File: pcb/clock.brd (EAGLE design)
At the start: 76.2 x 25.4 mm, 20 parts, among them IC1 74AHCT125, U1 ESP-01, U2 LD1117V33

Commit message: Added DTR to RST pin
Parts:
- added C5: 0.1uF, rcl:C025-025X050
- added R7: 10K, rcl:0207/10
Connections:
- removed net N$2: R2.1, U1.B2, U1.C2
- new net N$4: R2.1, U1.B2
- new net RESET: C5.1, R7.1, U1.C2
- net DTR: now also C5.2
- net VCC: now also R7.2
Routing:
- net DTR: track 0.00 -> 34.4 mm
- net RESET: track 0.00 -> 18.5 mm
- net N$4: track 0.00 -> 13.8 mm
- net N$2: track 13.8 -> 0.00 mm
- net VCC: track 57.1 -> 60.3 mm
- net GPIO0: track 32.8 -> 31.8 mm
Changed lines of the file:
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@@
 <setting verticaltext="up"/>
 </settings>
-<grid distance="0.05" unitdist="inch" unit="inch" style="lines" multiple="1" display="yes" altdistance="0.025" altunitdist="inch" altunit="inch"/>
+<grid distance="0.05" unitdist="inch" unit="inch" style="lines" multiple="1" display="yes" altdistance="0.005" altunitdist="inch" altunit="inch"/>
 <layers>
 <layer number="1" name="Top" color="4" fill="1" visible="yes" active="yes"/>
@@
 <element name="H1" library="holes" package="2,8-PAD" value="MOUNT-PAD-ROUND2.8" x="62.865" y="20.32"/>
 <element name="H2" library="holes" package="2,8-PAD-SQUARE" value="MOUNT-PAD-SQUARE2.8" x="71.12" y="20.32"/>
-<element name="D1" library="diode" package="DO41-7.6" value="1N5817-B" x="20.32" y="9.525" rot="R180"/>
+<element name="D1" library="diode" package="DO41-7.6" value="1N5817-B" x="20.32" y="9.525" smashed="yes" rot="R180"/>
+<element name="R7" library="rcl" package="0207/10" value="10K" x="40.64" y="8.89" smashed="yes">
+<attribute name="VALUE" x="38.3794" y="8.255" size="1.27" layer="27" ratio="10"/>
+</element>
+<element name="C5" library="rcl" package="C025-025X050" value="0.1uF" x="33.02" y="8.89" smashed="yes" rot="R270"/>
 </elements>
 <signals>
@@
 <wire x1="51.435" y1="5.715" x2="52.07" y2="5.08" width="0.4064" layer="1"/>
 <wire x1="45.72" y1="2.54" x2="45.72" y2="5.715" width="0.4064" layer="1"/>
+<contactref element="R7" pad="2"/>
+<wire x1="45.72" y1="8.89" x2="45.72" y2="5.715" width="0.4064" layer="1"/>
 </signal>
 <signal name="+5V">
@@
 <signal name="DTR">
 <contactref element="JP1" pad="6"/>
+<contactref element="C5" pad="2"/>
+<wire x1="2.54" y1="5.08" x2="2.54" y2="3.81" width="0.4064" layer="16"/>
+<wire x1="2.54" y1="3.81" x2="3.81" y2="2.54" width="0.4064" layer="16"/>
+<wire x1="3.81" y1="2.54" x2="17.78" y2="2.54" width="0.4064" layer="16"/>
+<wire x1="17.78" y1="2.54" x2="19.05" y2="3.81" width="0.4064" layer="16"/>
+<wire x1="19.05" y1="3.81" x2="29.21" y2="3.81" width="0.4064" layer="16"/>
+<wire x1="29.21" y1="3.81" x2="33.02" y2="7.62" width="0.4064" layer="16"/>
 </signal>
 <signal name="RXD_3V3">
@@
 <wire x1="24.13" y1="22.86" x2="26.67" y2="20.32" width="0.4064" layer="16"/>
 </signal>
-<signal name="N$2">
-<contactref element="U1" pad="B2"/>
-<contactref element="R2" pad="1"/>
-<contactref element="U1" pad="C2"/>
-<wire x1="22.86" y1="2.54" x2="25.4" y2="2.54" width="0.4064" layer="1"/>
-<wire x1="25.4" y1="2.54" x2="26.67" y2="3.81" width="0.4064" layer="1"/>
-<wire x1="26.67" y1="3.81" x2="34.29" y2="3.81" width="0.4064" layer="1"/>
-<wire x1="34.29" y1="3.81" x2="35.56" y2="2.54" width="0.4064" layer="1"/>
-</signal>
 <signal name="N$3">
 <contactref element="R4" pad="1"/>
@@
 <contactref element="R6" pad="1"/>
 <wire x1="6.275" y1="9.18" x2="12.775" y2="9.18" width="0.4064" layer="16"/>
-<wire x1="25.4" y1="5.08" x2="27.94" y2="7.62" width="0.4064" layer="1"/>
-<wire x1="27.94" y1="7.62" x2="33.655" y2="7.62" width="0.4064" layer="1"/>
-<wire x1="33.655" y1="7.62" x2="35.56" y2="5.715" width="0.4064" layer="1"/>
 <wire x1="12.775" y1="9.18" x2="14.335" y2="7.62" width="0.4064" layer="16"/>
 <wire x1="14.335" y1="7.62" x2="22.86" y2="7.62" width="0.4064" layer="16"/>
 <wire x1="22.86" y1="7.62" x2="25.4" y2="5.08" width="0.4064" layer="16"/>
+<wire x1="25.4" y1="5.08" x2="26.67" y2="6.35" width="0.4064" layer="1"/>
+<wire x1="26.67" y1="6.35" x2="34.925" y2="6.35" width="0.4064" layer="1"/>
+<wire x1="34.925" y1="6.35" x2="35.56" y2="5.715" width="0.4064" layer="1"/>
 </signal>
 <signal name="+5V_FTDI">
@@
 <wire x1="14.605" y1="7.62" x2="16.51" y2="9.525" width="0.4064" layer="1"/>
 </signal>
+<signal name="N$4">
+<contactref element="R2" pad="1"/>
+<contactref element="U1" pad="B2"/>
+<wire x1="35.56" y1="2.54" x2="34.29" y2="3.81" width="0.4064" layer="1"/>
+<wire x1="34.29" y1="3.81" x2="24.13" y2="3.81" width="0.4064" layer="1"/>
+<wire x1="24.13" y1="3.81" x2="22.86" y2="2.54" width="0.4064" layer="1"/>
+</signal>
+<signal name="RESET">
+<contactref element="U1" pad="C2"/>
+<contactref element="R7" pad="1"/>
+<contactref element="C5" pad="1"/>
+<wire x1="33.02" y1="10.16" x2="34.29" y2="10.16" width="0.4064" layer="1"/>
+<wire x1="34.29" y1="10.16" x2="35.56" y2="8.89" width="0.4064" layer="1"/>
+<wire x1="25.4" y1="2.54" x2="26.67" y2="1.27" width="0.254" layer="16"/>
+<wire x1="26.67" y1="1.27" x2="29.21" y2="1.27" width="0.254" layer="16"/>
+<wire x1="29.21" y1="1.27" x2="31.75" y2="3.81" width="0.254" layer="16"/>
+<wire x1="31.75" y1="3.81" x2="31.75" y2="5.334" width="0.254" layer="16"/>
+<wire x1="31.75" y1="5.334" x2="32.766" y2="6.35" width="0.254" layer="16"/>
+<wire x1="32.766" y1="6.35" x2="34.163" y2="6.35" width="0.254" layer="16"/>
+<wire x1="34.163" y1="6.35" x2="35.56" y2="7.747" width="0.254" layer="16"/>
+<wire x1="35.56" y1="7.747" x2="35.56" y2="8.89" width="0.254" layer="16"/>
+</signal>
 </signals>

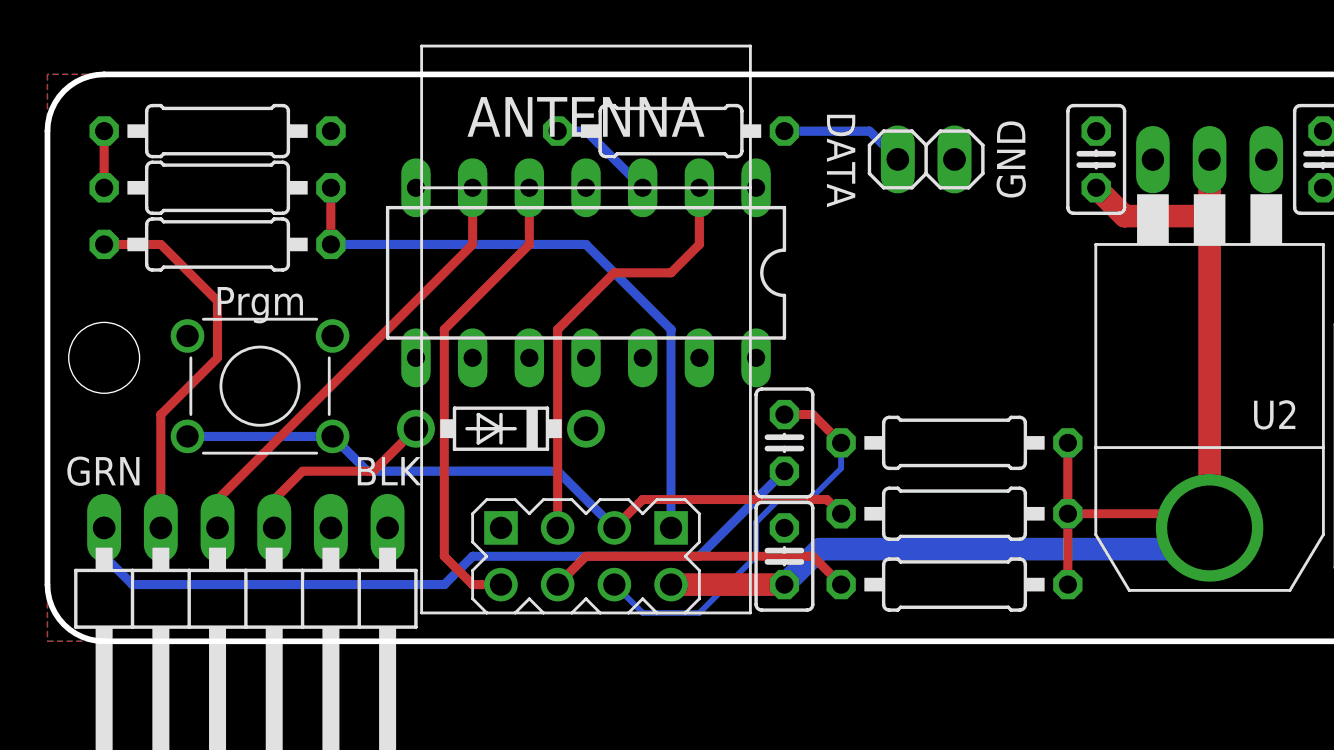
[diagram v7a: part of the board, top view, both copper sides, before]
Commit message: Changed resistor size & voltage divider values
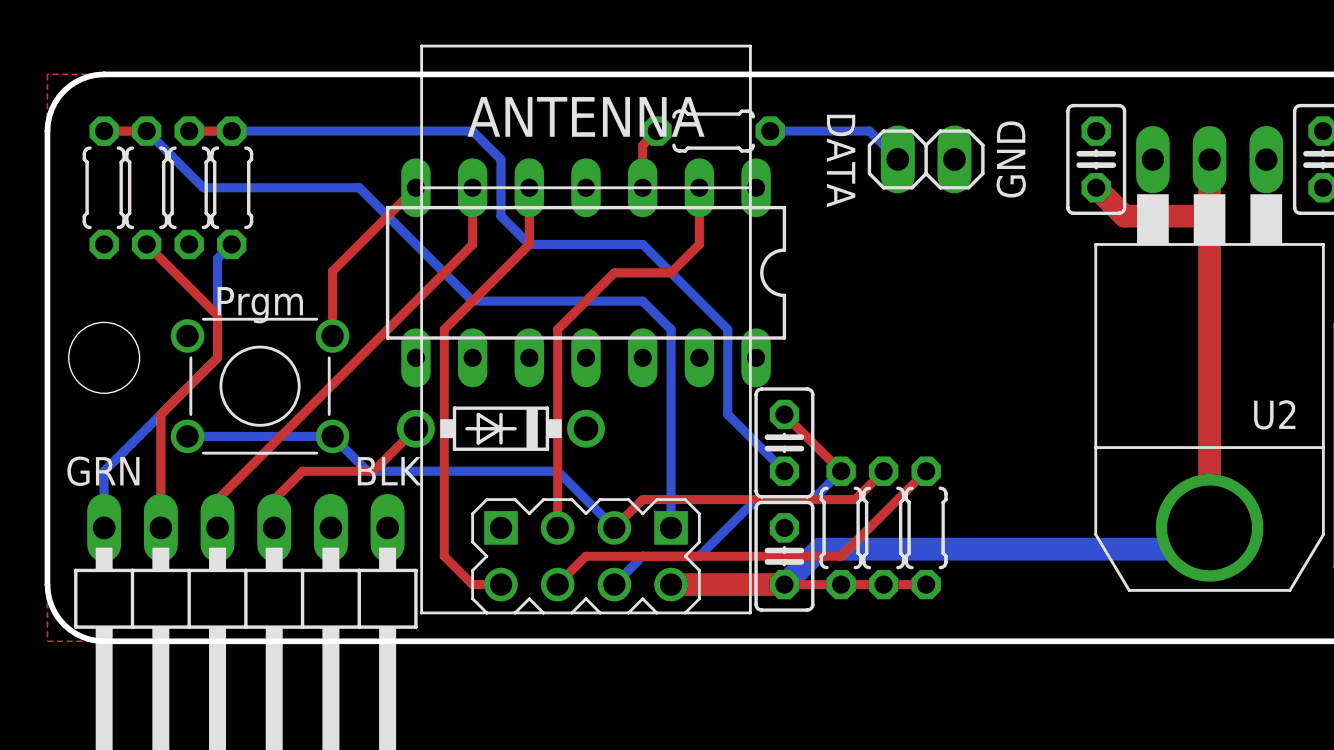
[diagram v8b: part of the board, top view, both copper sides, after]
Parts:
- added R8: 3.3K, rcl:0204/5
- R1, R2, R6, R7: device rcl:0207/10 -> rcl:0204/5
- R3, R5: value 470 -> 1.8K; device rcl:0207/10 -> rcl:0204/5
- R4: value 470 -> 3.3K; device rcl:0207/10 -> rcl:0204/5
- moved R7 6.35 mm to (35.6, 5.08), turned to 270 degrees
- moved R4 5.08 mm to (2.54, 20.3), turned to 90 degrees
- moved R3 4.07 mm to (4.45, 20.3), turned to 270 degrees
- moved R6 3.24 mm to (37.5, 5.08), turned to 270 degrees
- moved R2 2.84 mm to (39.4, 5.08), turned to 270 degrees
- moved R5 2.62 mm to (8.26, 20.3), turned to 270 degrees
- moved R1 1.90 mm to (29.8, 22.9)
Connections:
- removed net N$3: R4.1, R5.2
- new net N$2: C5.2, R5.1, R8.2
- net DTR: now also R5.2; no longer C5.2
- net GND: now also R4.1, R8.1; no longer R5.1
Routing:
- net N$2: track 0.00 -> 36.7 mm
- net DTR: track 34.4 -> 15.1 mm
- net RXD_3V3: track 28.2 -> 38.0 mm
- net GND: track 0.00 -> 8.19 mm
- net VCC: track 60.3 -> 54.5 mm
- net N$4: track 13.8 -> 18.6 mm
- net RESET: track 18.5 -> 15.9 mm
- net N$3: track 2.54 -> 0.00 mm
- net RXD_5V: track 17.3 -> 15.1 mm
- net GPIO0: track 31.8 -> 33.9 mm
- net NP_DATA: track 4.86 -> 2.80 mm
- net N$1: track 5.61 -> 6.24 mm
